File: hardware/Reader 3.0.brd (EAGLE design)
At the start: 55.9 x 58.4 mm, 10 parts, among them U1 ESP32-DEVKITC-32DHEADERS_ONLY

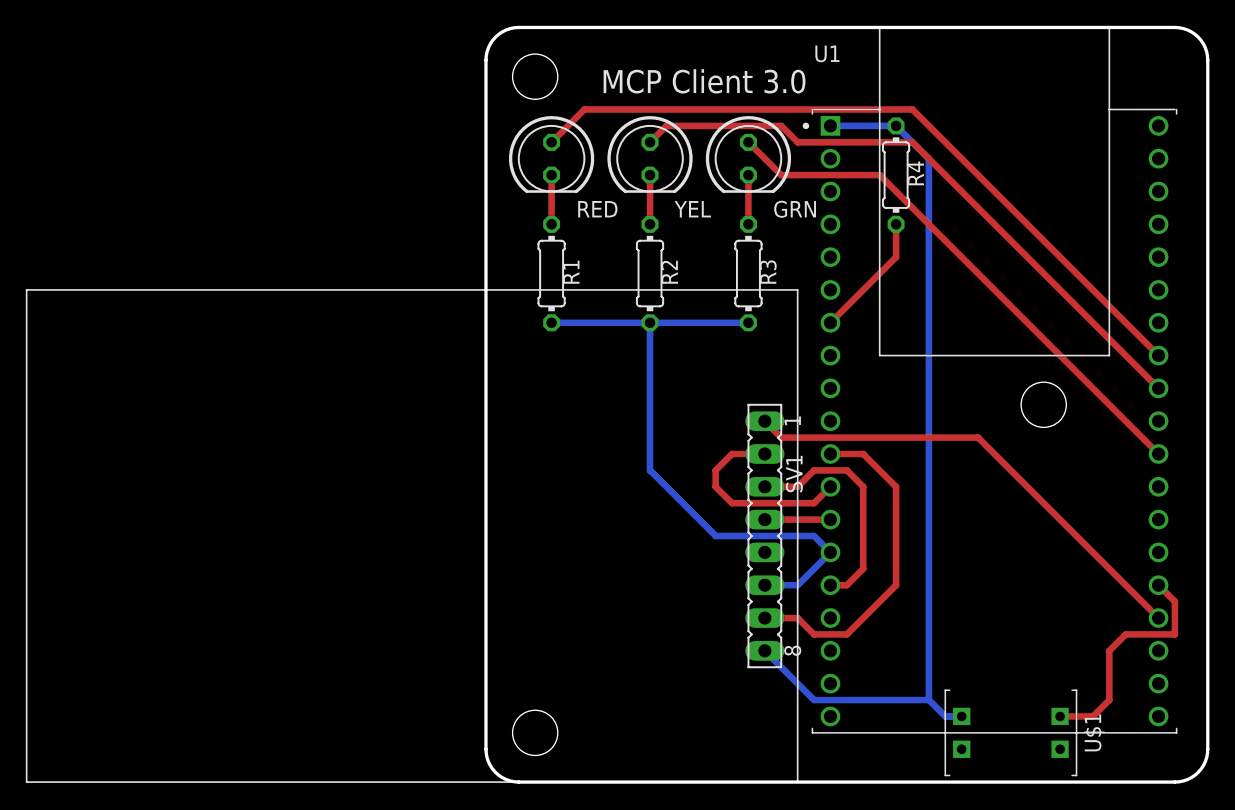
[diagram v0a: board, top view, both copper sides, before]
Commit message: add rj45 jack to board
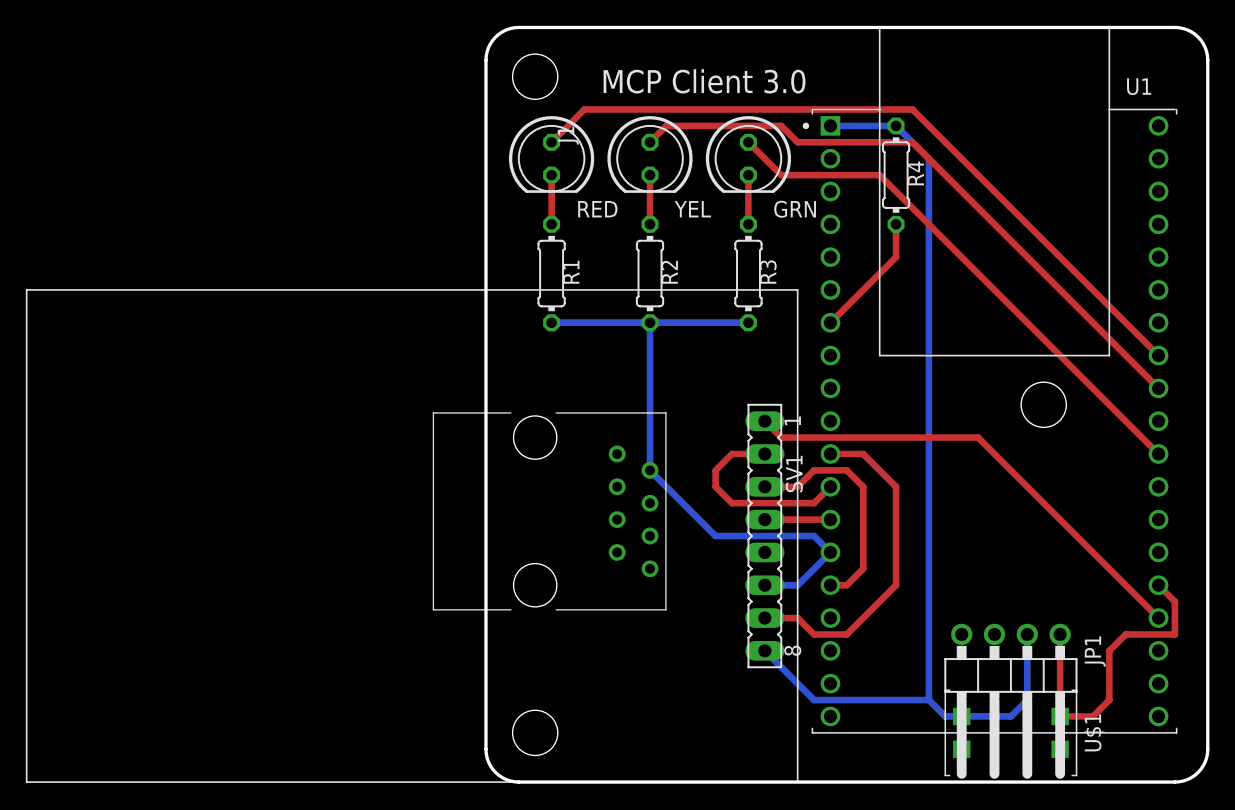
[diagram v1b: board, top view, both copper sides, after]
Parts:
- added J1: 54601-908WPLFW/MODEL, mcp:HDRV4W64P254_1X4_1016X508X838B
- added JP1: (no value), mcp:1X04/90
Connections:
- net +3V3: now also JP1.2
- net IO2: now also JP1.1
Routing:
- net +3V3: track 67.9 -> 78.6 mm
- net IO2: track 18.1 -> 24.4 mm

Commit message: Assign jack pins
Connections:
- removed net EXT_5V: U1.19
- new net +5V: J1.1, J1.5, U1.19
- new net N$10: J1.6
- new net N$7: J1.2
- new net N$8: J1.7
- net GND: now also J1.4, J1.8
- net RELAY_OUT: now also J1.3, U1.8; no longer U1.21
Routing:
- net +5V: track 0.00 -> 40.5 mm
- net RELAY_OUT: track 0.00 -> 26.2 mm
- net GND: track 49.4 -> 54.0 mm
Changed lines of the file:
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@@
 <drawing>
 <settings>
-<setting alwaysvectorfont="yes"/>
+<setting alwaysvectorfont="no"/>
 <setting verticaltext="up"/>
 </settings>
@@
 </elements>
 <signals>
-<signal name="EXT_5V">
-<contactref element="U1" pad="19"/>
-</signal>
 <signal name="SDA">
 <contactref element="SV1" pad="1"/>
@@
 <contactref element="R1" pad="2"/>
 <contactref element="SV1" pad="6"/>
-<wire x1="21.59" y1="15.24" x2="24.13" y2="15.24" width="0.508" layer="16"/>
-<wire x1="24.13" y1="15.24" x2="26.67" y2="17.78" width="0.508" layer="16"/>
-<wire x1="26.67" y1="17.78" x2="25.4" y2="19.05" width="0.508" layer="16"/>
-<wire x1="25.4" y1="19.05" x2="17.78" y2="19.05" width="0.508" layer="16"/>
-<wire x1="17.78" y1="19.05" x2="12.7" y2="24.13" width="0.508" layer="16"/>
-<wire x1="12.7" y1="24.13" x2="12.7" y2="35.56" width="0.508" layer="16"/>
-<wire x1="20.32" y1="35.56" x2="12.7" y2="35.56" width="0.508" layer="16"/>
-<wire x1="12.7" y1="35.56" x2="5.08" y2="35.56" width="0.508" layer="16"/>
+<wire x1="21.59" y1="15.24" x2="24.13" y2="15.24" width="1.016" layer="16"/>
+<wire x1="24.13" y1="15.24" x2="26.67" y2="17.78" width="1.016" layer="16"/>
+<wire x1="20.32" y1="35.56" x2="17.78" y2="35.56" width="1.016" layer="16"/>
+<wire x1="17.78" y1="35.56" x2="12.7" y2="35.56" width="1.016" layer="16"/>
+<wire x1="12.7" y1="35.56" x2="5.08" y2="35.56" width="1.016" layer="16"/>
+<contactref element="J1" pad="8"/>
+<contactref element="J1" pad="4"/>
+<wire x1="17.78" y1="19.05" x2="15.24" y2="16.51" width="1.016" layer="16"/>
+<wire x1="15.24" y1="16.51" x2="12.7" y2="16.51" width="1.016" layer="16"/>
+<wire x1="12.7" y1="16.51" x2="11.43" y2="16.51" width="1.016" layer="16"/>
+<wire x1="11.43" y1="16.51" x2="10.16" y2="17.78" width="1.016" layer="16"/>
+<wire x1="17.78" y1="19.05" x2="17.78" y2="35.56" width="1.016" layer="16"/>
+<wire x1="17.78" y1="19.05" x2="17.78" y2="16.51" width="1.016" layer="16"/>
+<wire x1="17.78" y1="16.51" x2="19.05" y2="15.24" width="1.016" layer="16"/>
+<wire x1="19.05" y1="15.24" x2="21.59" y2="15.24" width="1.016" layer="16"/>
 <wire x1="52.07" y1="35.56" x2="52.07" y2="50.8" width="0" layer="19" extent="1-1"/>
 <wire x1="26.67" y1="17.78" x2="52.07" y2="35.56" width="0" layer="19" extent="1-1"/>
@@
 </signal>
 <signal name="RELAY_OUT">
-<contactref element="U1" pad="21"/>
+<contactref element="J1" pad="3"/>
+<wire x1="10.16" y1="20.32" x2="15.24" y2="20.32" width="0.508" layer="1"/>
+<wire x1="15.24" y1="20.32" x2="16.51" y2="21.59" width="0.508" layer="1"/>
+<wire x1="16.51" y1="21.59" x2="16.51" y2="29.21" width="0.508" layer="1"/>
+<contactref element="U1" pad="8"/>
+<wire x1="16.51" y1="29.21" x2="20.32" y2="33.02" width="0.508" layer="1"/>
+<wire x1="20.32" y1="33.02" x2="26.67" y2="33.02" width="0.508" layer="1"/>
 </signal>
 <signal name="IO2">
@@
 <wire x1="44.45" y1="5.08" x2="44.45" y2="11.43" width="0.508" layer="1"/>
 </signal>
+<signal name="N$10">
+<contactref element="J1" pad="6"/>
+</signal>
+<signal name="N$7">
+<contactref element="J1" pad="2"/>
+</signal>
+<signal name="N$8">
+<contactref element="J1" pad="7"/>
+</signal>
+<signal name="+5V">
+<contactref element="J1" pad="1"/>
+<contactref element="J1" pad="5"/>
+<contactref element="U1" pad="19"/>
+<wire x1="26.67" y1="5.08" x2="12.7" y2="5.08" width="1.016" layer="16"/>
+<wire x1="12.7" y1="5.08" x2="7.62" y2="10.16" width="1.016" layer="16"/>
+<wire x1="7.62" y1="10.16" x2="7.62" y2="22.86" width="1.016" layer="16"/>
+<wire x1="7.62" y1="22.86" x2="10.16" y2="25.4" width="1.016" layer="16"/>
+<wire x1="10.16" y1="25.4" x2="11.43" y2="25.4" width="1.016" layer="16"/>
+<wire x1="11.43" y1="25.4" x2="12.7" y2="24.13" width="1.016" layer="16"/>
+</signal>
 </signals>

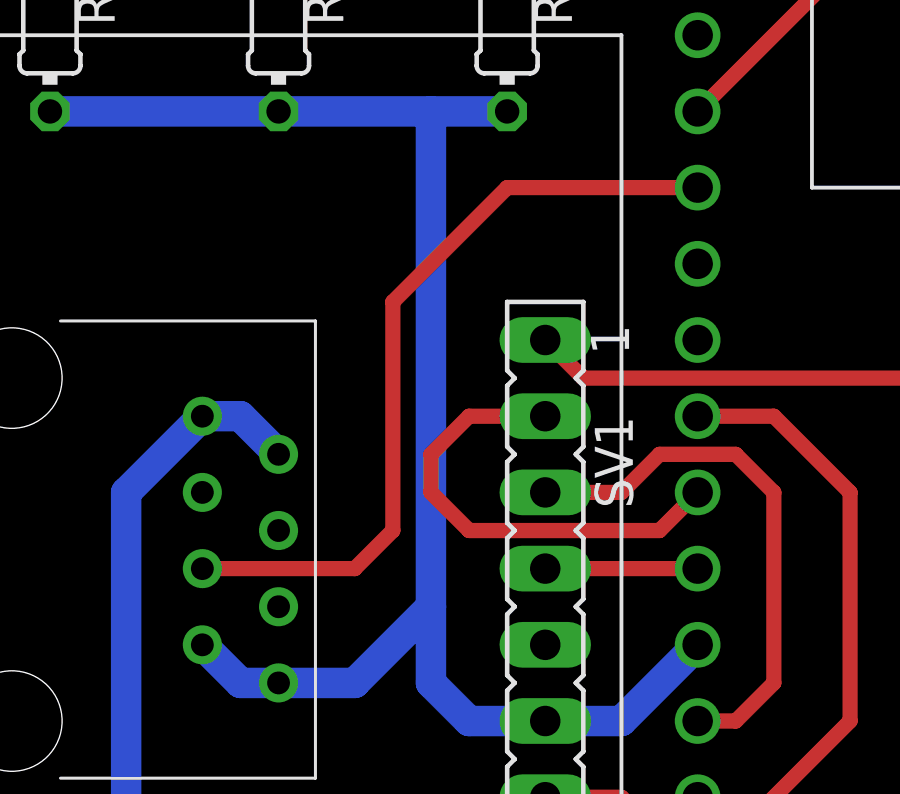
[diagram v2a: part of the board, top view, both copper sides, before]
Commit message: add current sense input
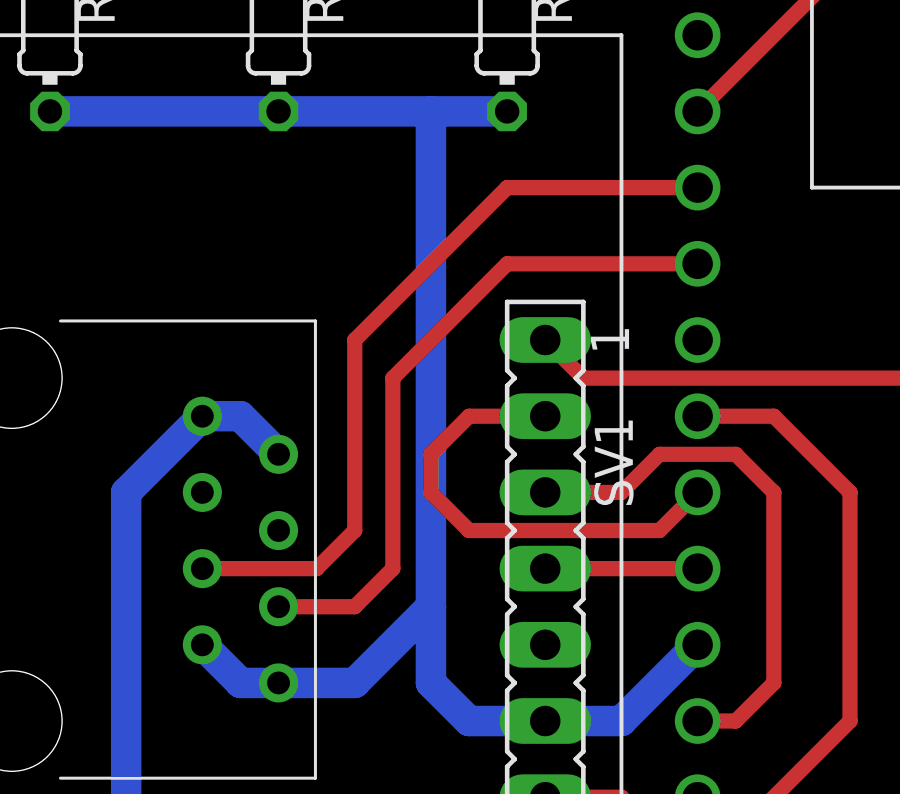
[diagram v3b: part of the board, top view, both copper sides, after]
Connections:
- removed net N$8: J1.7
- new net CURRENT_IN: J1.7, U1.9
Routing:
- net CURRENT_IN: track 0.00 -> 22.4 mm
- net RELAY_OUT: track 26.2 -> 25.5 mm
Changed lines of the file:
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@@
 <signal name="RELAY_OUT">
 <contactref element="J1" pad="3"/>
-<wire x1="10.16" y1="20.32" x2="15.24" y2="20.32" width="0.508" layer="1"/>
-<wire x1="15.24" y1="20.32" x2="16.51" y2="21.59" width="0.508" layer="1"/>
-<wire x1="16.51" y1="21.59" x2="16.51" y2="29.21" width="0.508" layer="1"/>
+<wire x1="10.16" y1="20.32" x2="13.97" y2="20.32" width="0.508" layer="1"/>
+<wire x1="13.97" y1="20.32" x2="15.24" y2="21.59" width="0.508" layer="1"/>
+<wire x1="15.24" y1="21.59" x2="15.24" y2="27.94" width="0.508" layer="1"/>
 <contactref element="U1" pad="8"/>
-<wire x1="16.51" y1="29.21" x2="20.32" y2="33.02" width="0.508" layer="1"/>
+<wire x1="15.24" y1="27.94" x2="20.32" y2="33.02" width="0.508" layer="1"/>
 <wire x1="20.32" y1="33.02" x2="26.67" y2="33.02" width="0.508" layer="1"/>
 </signal>
@@
 <contactref element="J1" pad="2"/>
 </signal>
-<signal name="N$8">
-<contactref element="J1" pad="7"/>
-</signal>
 <signal name="+5V">
 <contactref element="J1" pad="1"/>
@@
 <wire x1="11.43" y1="25.4" x2="12.7" y2="24.13" width="1.016" layer="16"/>
 </signal>
+<signal name="CURRENT_IN">
+<contactref element="U1" pad="9"/>
+<contactref element="J1" pad="7"/>
+<wire x1="12.7" y1="19.05" x2="15.24" y2="19.05" width="0.508" layer="1"/>
+<wire x1="15.24" y1="19.05" x2="16.51" y2="20.32" width="0.508" layer="1"/>
+<wire x1="16.51" y1="20.32" x2="16.51" y2="26.67" width="0.508" layer="1"/>
+<wire x1="16.51" y1="26.67" x2="20.32" y2="30.48" width="0.508" layer="1"/>
+<wire x1="20.32" y1="30.48" x2="26.67" y2="30.48" width="0.508" layer="1"/>
+</signal>
 </signals>

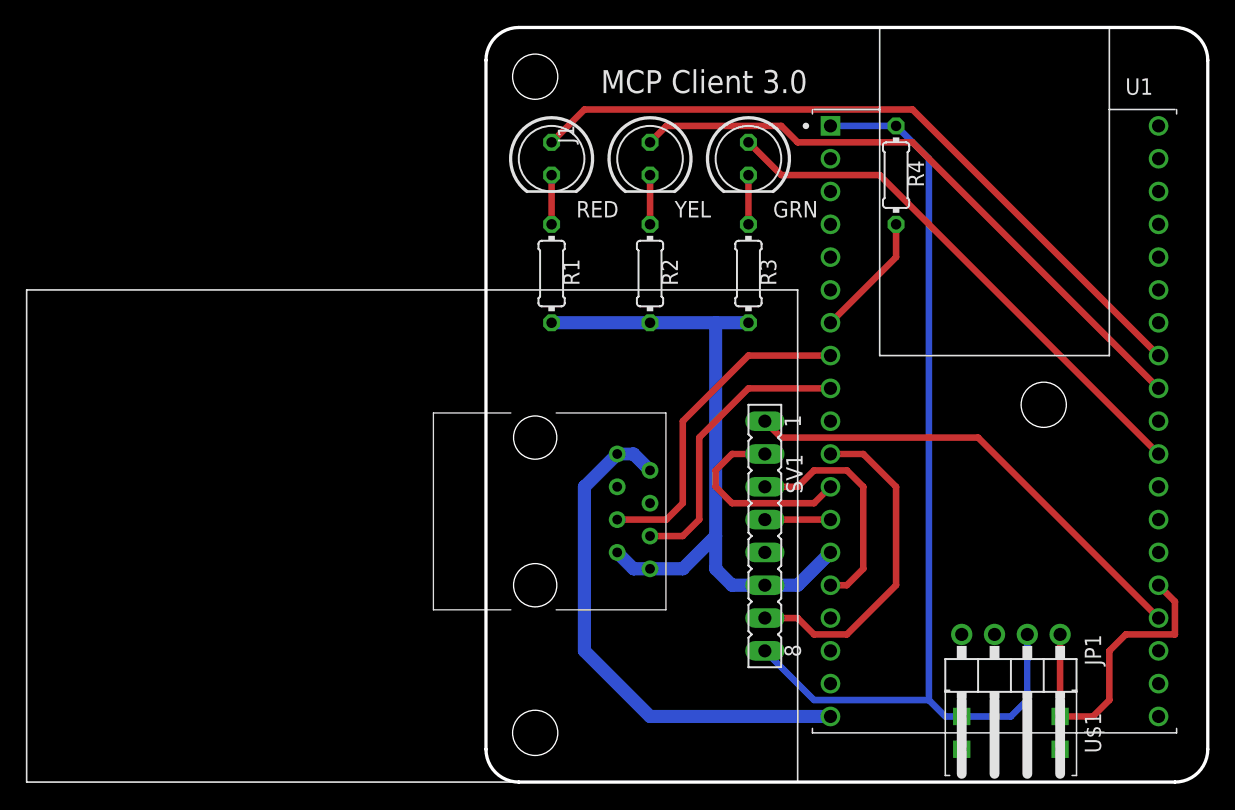
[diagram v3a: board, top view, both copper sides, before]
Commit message: Slight adjustments to board layout, add pullup resistor
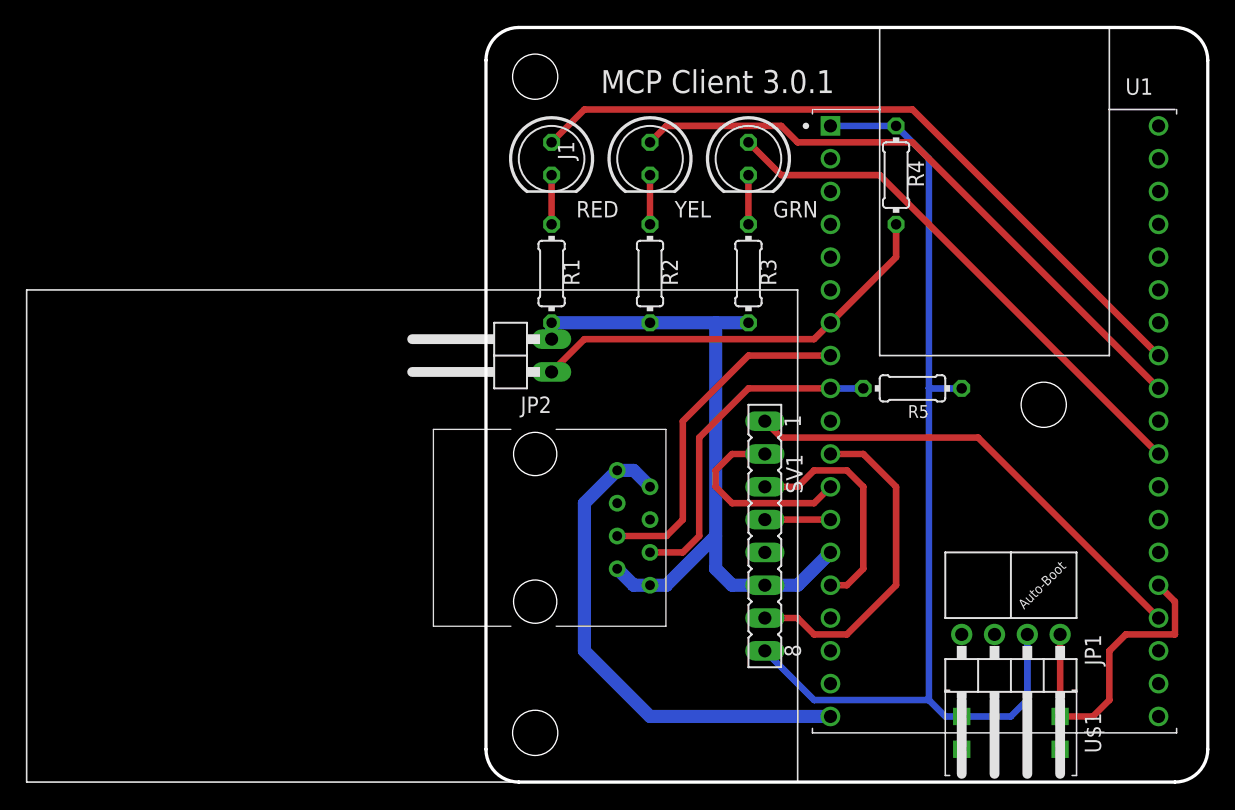
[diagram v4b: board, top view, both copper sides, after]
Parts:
- added JP2: (no value), mcp:1X02/90
- added R5: 10k, mcp:0204/7
- moved J1 1.27 mm to (10.2, 24.1)
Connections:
- net +3V3: now also R5.1
- net CURRENT_IN: now also R5.2
- net GND: now also JP2.2
- net POW_SW: now also JP2.1
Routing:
- net POW_SW: track 9.72 -> 32.9 mm
- net CURRENT_IN: track 22.4 -> 26.2 mm
- net +3V3: track 78.6 -> 81.2 mm
- net GND: track 54.0 -> 55.8 mm
- net RELAY_OUT: track 25.5 -> 26.8 mm
- net +5V: track 40.5 -> 39.2 mm
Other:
- board text added: "Auto-Boot"
- board text added: "MCP Client 3.0.1"
- board text removed: "MCP Client 3.0"

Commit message: change LED names in circuit layout
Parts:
- moved GRN 15.2 mm to (5.08, 48.3)
- moved RED 15.2 mm to (20.3, 48.3)
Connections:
- net N$1: now also RED.A; no longer GRN.A
- net N$3: now also GRN.A; no longer RED.A
- net N$4: now also GRN.K; no longer RED.K
- net N$6: now also RED.K; no longer GRN.K
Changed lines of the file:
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@@
 <drawing>
 <settings>
-<setting alwaysvectorfont="yes"/>
+<setting alwaysvectorfont="no"/>
 <setting verticaltext="up"/>
 </settings>
@@
 <attribute name="VALUE" x="18.669" y="29.21" size="1.27" layer="27" ratio="10" rot="R270"/>
 </element>
-<element name="GRN" library="led" library_urn="urn:adsk.eagle:library:259" package="LED5MM" package3d_urn="urn:adsk.eagle:package:15799/2" value="" x="20.32" y="48.26" smashed="yes" rot="R270">
+<element name="RED" library="led" library_urn="urn:adsk.eagle:library:259" package="LED5MM" package3d_urn="urn:adsk.eagle:package:15799/2" value="" x="20.32" y="48.26" smashed="yes" rot="R270">
 <attribute name="NAME" x="22.225" y="43.7134" size="1.27" layer="25" ratio="10"/>
 <attribute name="VALUE" x="18.5166" y="45.0596" size="1.27" layer="27" ratio="10" rot="R270"/>
@@
 <attribute name="VALUE" x="10.8966" y="45.0596" size="1.27" layer="27" ratio="10" rot="R270"/>
 </element>
-<element name="RED" library="led" library_urn="urn:adsk.eagle:library:259" package="LED5MM" package3d_urn="urn:adsk.eagle:package:15799/2" value="" x="5.08" y="48.26" smashed="yes" rot="R270">
-<attribute name="NAME" x="6.985" y="43.7134" size="1.27" layer="25" ratio="10"/>
+<element name="GRN" library="led" library_urn="urn:adsk.eagle:library:259" package="LED5MM" package3d_urn="urn:adsk.eagle:package:15799/2" value="" x="5.08" y="48.26" smashed="yes" rot="R270">
+<attribute name="NAME" x="5.715" y="43.7134" size="1.27" layer="25" ratio="10"/>
 <attribute name="VALUE" x="3.2766" y="45.0596" size="1.27" layer="27" ratio="10" rot="R270"/>
 </element>
@@
 </element>
 <element name="J1" library="mcp" library_urn="urn:adsk.eagle:library:9418757" package="HDRV4W64P254_1X4_1016X508X838B" package3d_urn="urn:adsk.eagle:package:9475071/4" value="54601-908WPLFW/MODEL" x="10.16" y="24.13" smashed="yes" rot="R270">
-<attribute name="NAME" x="6.2" y="48.895" size="1.27" layer="25" rot="R270" align="center"/>
+<attribute name="NAME" x="12.55" y="26.035" size="1.27" layer="25" rot="R270" align="center"/>
 <attribute name="VALUE" x="18.9" y="23.495" size="1.27" layer="27" rot="R270" align="center"/>
 </element>
@@
 <signal name="N$1">
 <contactref element="U1" pad="30"/>
-<contactref element="GRN" pad="A"/>
+<contactref element="RED" pad="A"/>
 <wire x1="30.48" y1="46.99" x2="22.86" y2="46.99" width="0.508" layer="1"/>
 <wire x1="22.86" y1="46.99" x2="20.32" y2="49.53" width="0.508" layer="1"/>
@@
 <signal name="N$3">
 <contactref element="U1" pad="27"/>
-<contactref element="RED" pad="A"/>
+<contactref element="GRN" pad="A"/>
 <wire x1="33.02" y1="52.07" x2="7.62" y2="52.07" width="0.508" layer="1"/>
 <wire x1="7.62" y1="52.07" x2="5.08" y2="49.53" width="0.508" layer="1"/>
@@
 </signal>
 <signal name="N$4">
-<contactref element="RED" pad="K"/>
+<contactref element="GRN" pad="K"/>
 <contactref element="R1" pad="1"/>
 <wire x1="5.08" y1="43.18" x2="5.08" y2="46.99" width="0.508" layer="1"/>
@@
 </signal>
 <signal name="N$6">
-<contactref element="GRN" pad="K"/>
+<contactref element="RED" pad="K"/>
 <contactref element="R3" pad="1"/>
 <wire x1="20.32" y1="43.18" x2="20.32" y2="46.99" width="0.508" layer="1"/>
